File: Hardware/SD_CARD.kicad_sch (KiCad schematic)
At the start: 0 parts

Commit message: Checkpoint
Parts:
- added C24: 100nF, Capacitor_SMD:C_0805_2012Metric, symbol Device:C_Small
- added J17: SD_Card, leptunKicadLib:SDP-09L-SG, symbol Connector:SD_Card
- added R11, R12, R13, R14, R15: 47K, Resistor_SMD:R_0805_2012Metric, symbol Device:R_Small
- added R16, R17: 1K, Resistor_SMD:R_1206_3216Metric, symbol Device:R_Small
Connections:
- new net: J17.10 (CARD_DETECT), R16.1
- new net: J17.11 (WRITE_PROTECT), R17.2
- new net CD: R16.2
- new net CK: J17.5 (CLK)
- new net CMD: J17.2 (CMD), R13.2
- new net D0: J17.7 (DAT0), R12.2
- new net D1: J17.8 (DAT1), R11.2
- new net D2: J17.9 (DAT2), R15.2
- new net D3: J17.1 (CD/DAT3), R14.2
- new net GND: C24.2, J17.12 (SHELL1), J17.13 (SHELL2), J17.3 (VSS), J17.6 (VSS)
- new net VDD: C24.1, J17.4 (VDD), R11.1, R12.1, R13.1, R14.1, R15.1
- new net WP: R17.1

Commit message: Checkpoint
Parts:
- C24: footprint Capacitor_SMD:C_0805_2012Metric -> (none)
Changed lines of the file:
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@@
       (effects (font (size 1.27 1.27)) (justify left))
     )
-    (property "Footprint" "Capacitor_SMD:C_0805_2012Metric" (at 142.24 62.23 0)
+    (property "Footprint" "" (at 142.24 62.23 0)
       (effects (font (size 1.27 1.27)) hide)
     )

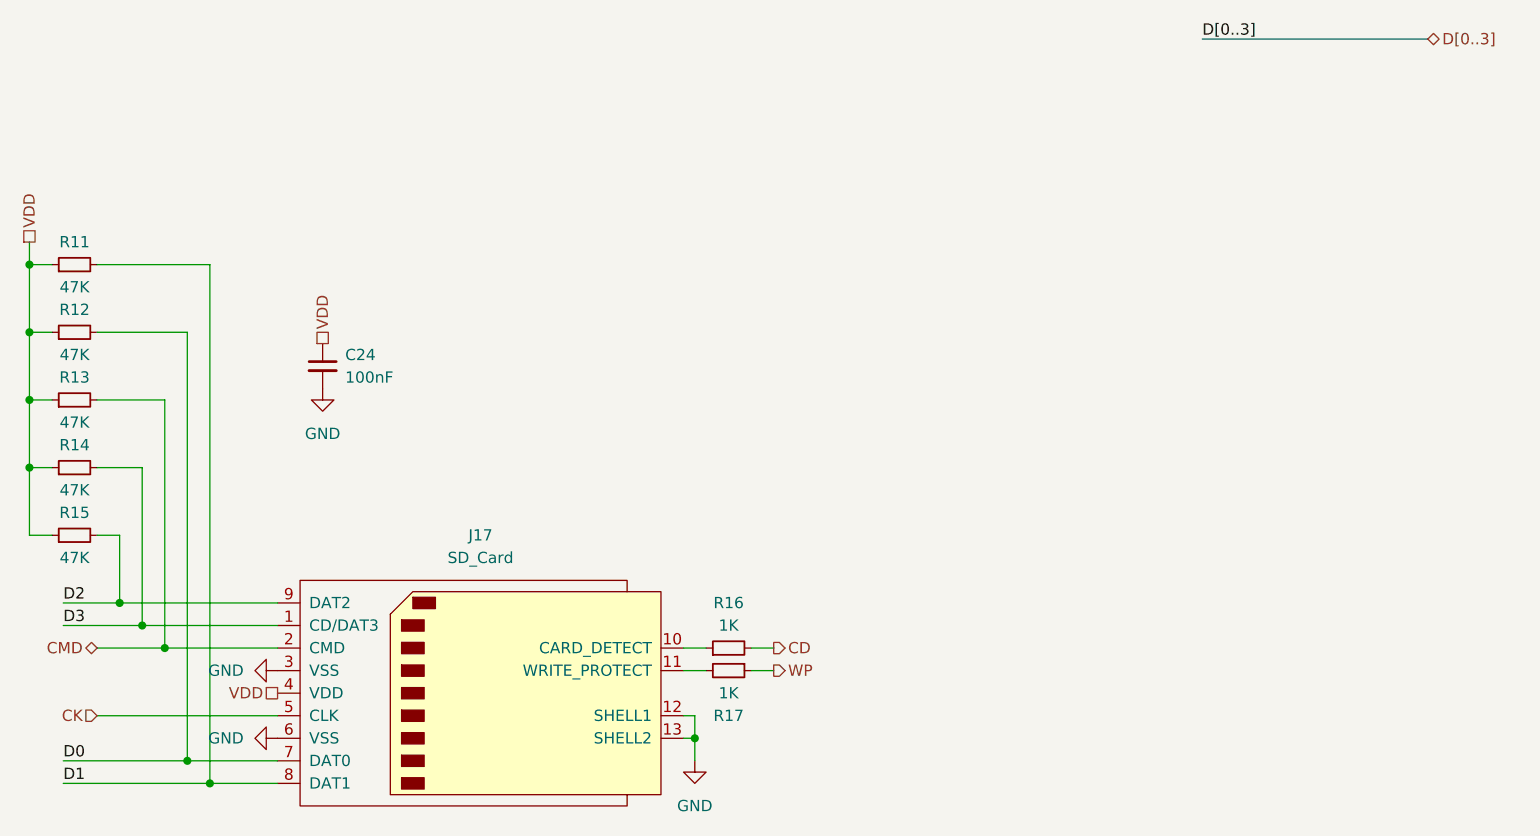
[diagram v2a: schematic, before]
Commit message: ERC fixes
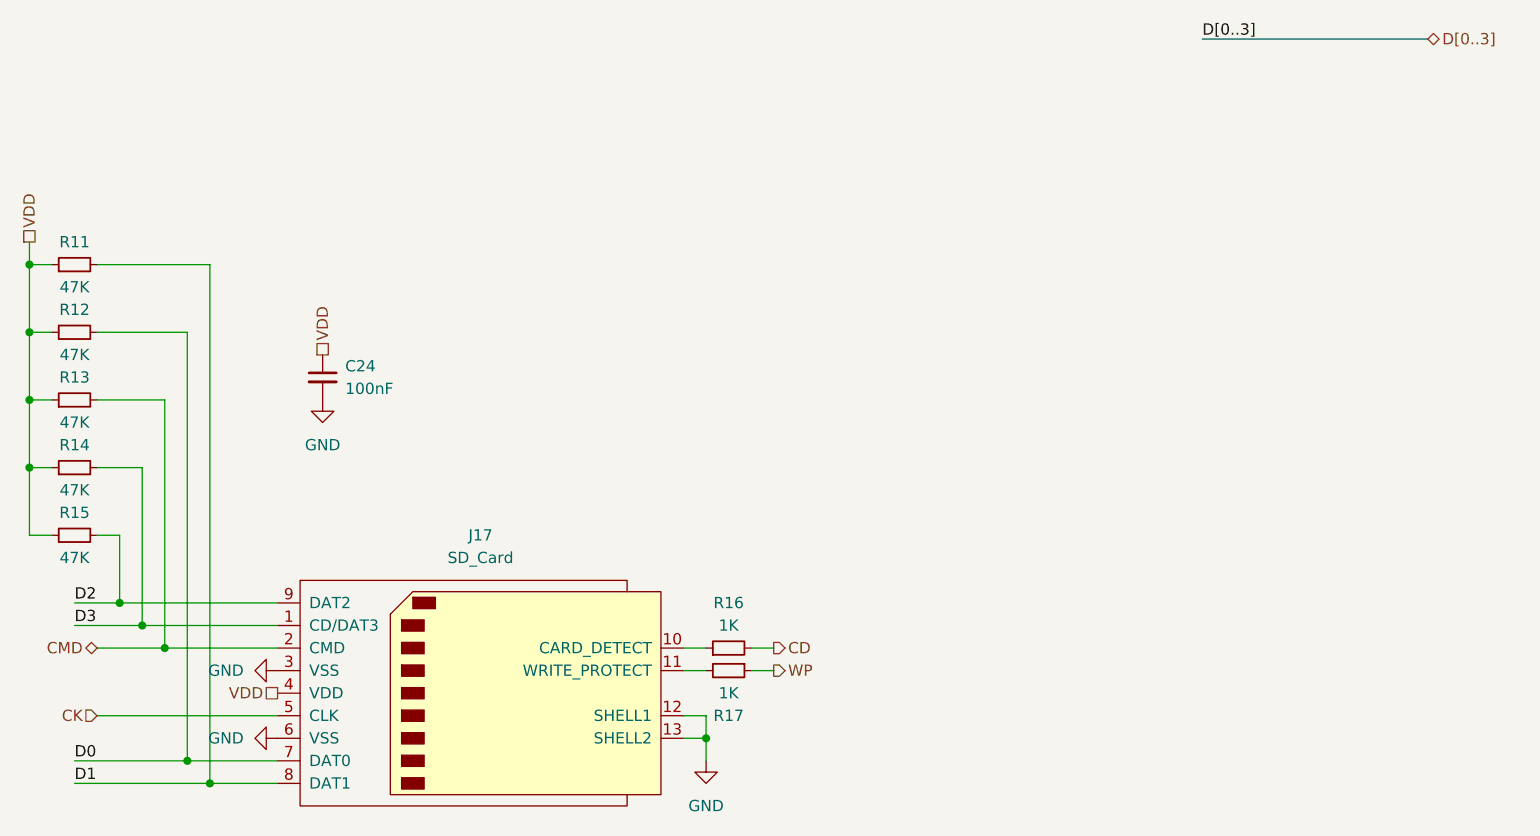
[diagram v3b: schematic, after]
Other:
- moved on the sheet: C24

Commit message: Checkpoint
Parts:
- R?: renamed from R11; footprint Resistor_SMD:R_0805_2012Metric -> (none)
- R?: renamed from R16; footprint Resistor_SMD:R_1206_3216Metric -> (none)
- R?: renamed from R17; footprint Resistor_SMD:R_1206_3216Metric -> (none)
- R?: renamed from R15; footprint Resistor_SMD:R_0805_2012Metric -> (none)
- R?: renamed from R13; footprint Resistor_SMD:R_0805_2012Metric -> (none)
- R?: renamed from R12; footprint Resistor_SMD:R_0805_2012Metric -> (none)
- R?: renamed from R14; footprint Resistor_SMD:R_0805_2012Metric -> (none)
- renumbered C24 to C?, J17 to J?

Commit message: Checkpoint
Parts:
- C?: footprint (none) -> Capacitor_SMD:C_0603_1608Metric
- R? (x5): footprint (none) -> Resistor_SMD:R_0805_2012Metric
- R? (x2): value 1K -> 2.2K; footprint (none) -> Resistor_SMD:R_0805_2012Metric
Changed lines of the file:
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@@
       (effects (font (size 1.27 1.27)))
     )
-    (property "Footprint" "" (at 114.3 50.8 0)
+    (property "Footprint" "Resistor_SMD:R_0805_2012Metric" (at 114.3 50.8 0)
       (effects (font (size 1.27 1.27)) hide)
     )
@@
       (effects (font (size 1.27 1.27)))
     )
-    (property "Value" "1K" (at 187.96 91.44 90)
-      (effects (font (size 1.27 1.27)))
-    )
-    (property "Footprint" "" (at 187.96 93.98 0)
+    (property "Value" "2.2K" (at 187.96 91.44 90)
+      (effects (font (size 1.27 1.27)))
+    )
+    (property "Footprint" "Resistor_SMD:R_0805_2012Metric" (at 187.96 93.98 0)
       (effects (font (size 1.27 1.27)) hide)
     )
@@
       (effects (font (size 1.27 1.27)))
     )
-    (property "Value" "1K" (at 187.96 99.06 90)
-      (effects (font (size 1.27 1.27)))
-    )
-    (property "Footprint" "" (at 187.96 96.52 0)
+    (property "Value" "2.2K" (at 187.96 99.06 90)
+      (effects (font (size 1.27 1.27)))
+    )
+    (property "Footprint" "Resistor_SMD:R_0805_2012Metric" (at 187.96 96.52 0)
       (effects (font (size 1.27 1.27)) hide)
     )
@@
       (effects (font (size 1.27 1.27)))
     )
-    (property "Footprint" "" (at 114.3 81.28 0)
+    (property "Footprint" "Resistor_SMD:R_0805_2012Metric" (at 114.3 81.28 0)
       (effects (font (size 1.27 1.27)) hide)
     )
@@
       (effects (font (size 1.27 1.27)) (justify left))
     )
-    (property "Footprint" "" (at 142.24 63.5 0)
+    (property "Footprint" "Capacitor_SMD:C_0603_1608Metric" (at 142.24 63.5 0)
       (effects (font (size 1.27 1.27)) hide)
     )
@@
       (effects (font (size 1.27 1.27)))
     )
-    (property "Footprint" "" (at 114.3 66.04 0)
+    (property "Footprint" "Resistor_SMD:R_0805_2012Metric" (at 114.3 66.04 0)
       (effects (font (size 1.27 1.27)) hide)
     )
@@
       (effects (font (size 1.27 1.27)))
     )
-    (property "Footprint" "" (at 114.3 58.42 0)
+    (property "Footprint" "Resistor_SMD:R_0805_2012Metric" (at 114.3 58.42 0)
       (effects (font (size 1.27 1.27)) hide)
     )
@@
       (effects (font (size 1.27 1.27)))
     )
-    (property "Footprint" "" (at 114.3 73.66 0)
-      (effects (font (size 1.27 1.27)) hide)
-    )
+    (property "Footprint" "Resistor_SMD:R_0805_2012Metric" (at 114.3 73.66 0)
+      (effects (font (size 1.27 1.27)) hide)
+    )

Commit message: Finalize silkscreen
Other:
- title: (none) -> Avionus_Flight_Controller
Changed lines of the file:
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@@
 (kicad_sch (version 20230121) (generator eeschema)
   (paper "A4")
+  (title_block
+    (title "Avionus_Flight_Controller")
+    (date "2023-11-25")
+    (rev "1.0")
+  )
   (junction (at 109.22 58.42) (diameter 0) (color 0 0 0 0)
   )
